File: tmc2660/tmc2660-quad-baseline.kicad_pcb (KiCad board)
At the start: 4 copper layers, 125 x 40 mm, 79 parts, among them J1 Power, J100 0R, J2 DataIn, J200 0R, J300 0R, J400 0R, M0 Mount, M1 Mount, M100 Mount, M101 Mount, M200 Mount, M201 Mount, M300 Mount, M301 Mount, M400 Mount, M401 Mount, P100 Motor, P200 Motor, P300 Motor, P400 Motor, U100 TMC2660, U200 TMC2660, U300 TMC2660, U400 TMC2660

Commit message: Add bottom silkscreen.
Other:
- board text added: "%%gitversion%%"
- board text added: "http://quadrigotion.org/"
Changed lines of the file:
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@@
   (general
     (thickness 1.6)
-    (drawings 29)
+    (drawings 31)
     (tracks 189)
     (zones 0)
@@
     (effects (font (size 2.2 2.2) (thickness 0.4)))
   )
+  (gr_text http://quadrigotion.org/ (at 198.3645 94.732) (layer B.SilkS)
+    (effects (font (size 1.2 1.2) (thickness 0.2)) (justify left mirror))
+  )
+  (gr_text %%gitversion%% (at 112.5125 94.732) (layer B.SilkS)
+    (effects (font (size 1.2 1.2) (thickness 0.2)) (justify mirror))
+  )
   (gr_arc (start 211.2 61.934) (end 213.2 61.934) (angle -90) (layer Edge.Cuts) (width 0.1))

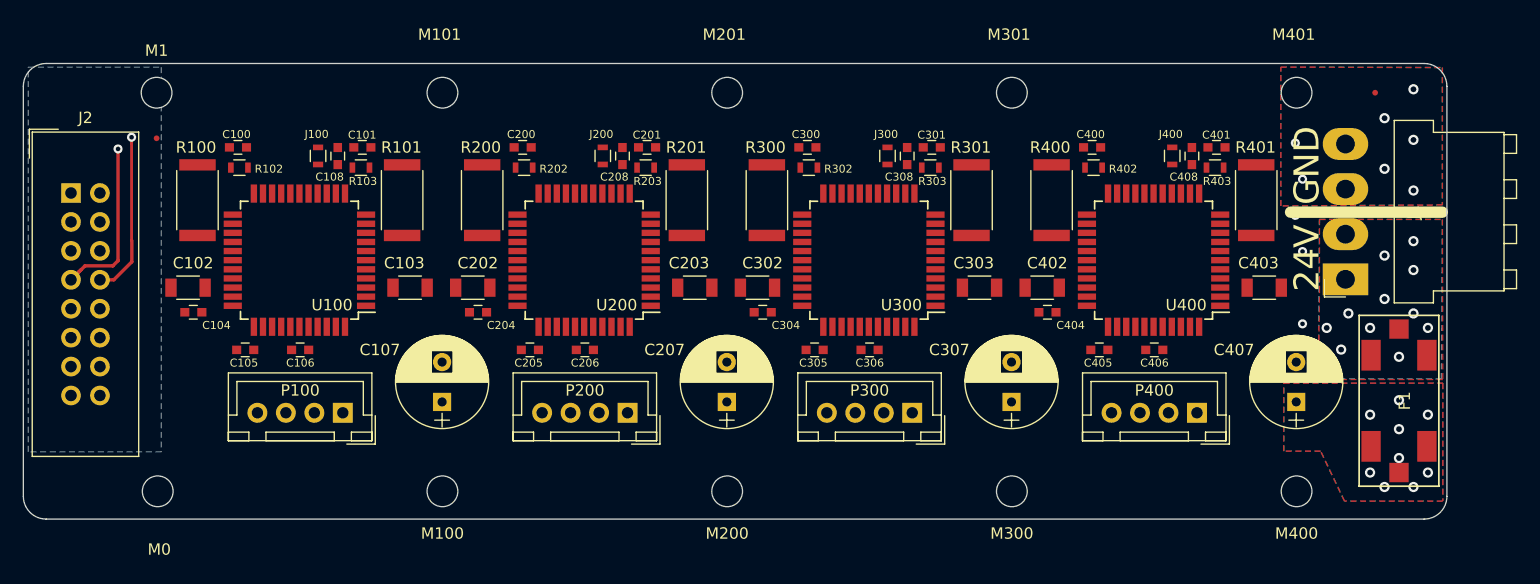
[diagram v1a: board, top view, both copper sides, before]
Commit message: Add front silkscreen. Re-add center fiducial.
o Front silkscreen and center fiducial got lost in the previous
  steps.
o Re-add in the baseline file and re-generate the final file.
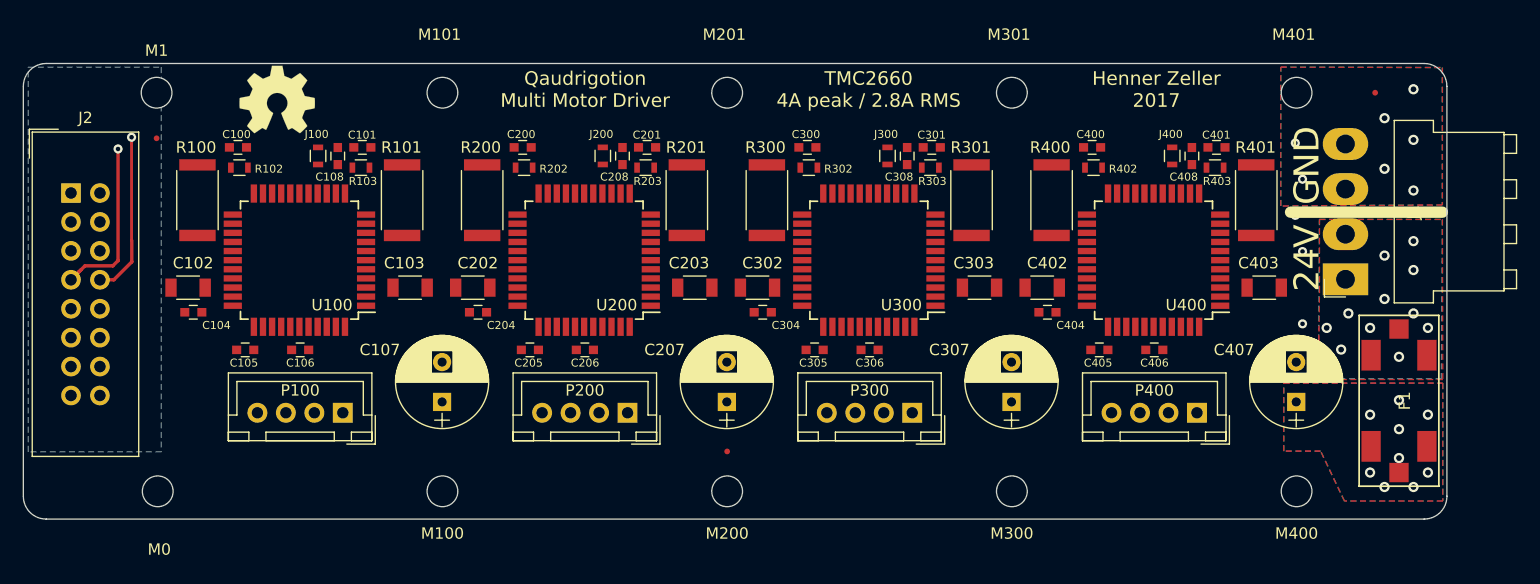
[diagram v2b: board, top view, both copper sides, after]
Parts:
- added REF**: Fiducial_0.5mm_Dia_1mm_Outer, Fiducials:Fiducial_0.5mm_Dia_1mm_Outer, F.Cu at (150.0, 94.0)
- added REF***: OSHW-Symbol_6.7x6mm_SilkScreen, Symbols:OSHW-Symbol_6.7x6mm_SilkScreen, F.Cu at (110.5, 63.1)
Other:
- board text added: "Henner Zeller 2017"
- board text added: "Qaudrigotion Multi Motor Driver"
- board text added: "TMC2660 4A peak / 2.8A RMS"

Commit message: GND plane around Step/Dir. Tighter routing of Step/Dir.
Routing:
- net DIR4: track 104.2 -> 104.8 mm
- net GND: vias 10 -> 9
- net GLOBAL_MOSI: vias 1 -> 2
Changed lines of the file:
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@@
     (thickness 1.6)
     (drawings 34)
-    (tracks 189)
+    (tracks 188)
     (zones 0)
     (modules 81)
@@
   (gr_line (start 88.2 97.939) (end 88.2 61.934) (layer Edge.Cuts) (width 0.1))
   (gr_line (start 211.2 99.939) (end 90.2 99.939) (layer Edge.Cuts) (width 0.1))
-  (via (at 199.8885 66.919) (size 0.8) (drill 0.4) (layers F.Cu B.Cu) (net 1))
+  (segment (start 189.7285 82.74601) (end 190.28449 83.302) (width 0.25) (layer In1.Cu) (net 51))
+  (segment (start 169.102489 84.497011) (end 170.85349 82.74601) (width 0.25) (layer In1.Cu) (net 51))
+  (segment (start 166.463458 83.82691) (end 167.133559 84.497011) (width 0.25) (layer In1.Cu) (net 51))
+  (segment (start 145.89659 83.82691) (end 166.463458 83.82691) (width 0.25) (layer In1.Cu) (net 51))
+  (segment (start 144.24559 85.47791) (end 145.89659 83.82691) (width 0.25) (layer In1.Cu) (net 51))
+  (segment (start 141.16511 85.47791) (end 144.24559 85.47791) (width 0.25) (layer In1.Cu) (net 51))
+  (segment (start 103.2721 84.4149) (end 104.519259 85.662059) (width 0.25) (layer In1.Cu) (net 51))
+  (segment (start 170.85349 82.74601) (end 189.7285 82.74601) (width 0.25) (layer In1.Cu) (net 51))
+  (segment (start 140.27611 84.58891) (end 141.16511 85.47791) (width 0.25) (layer In1.Cu) (net 51))
+  (segment (start 121.184452 84.58891) (end 140.27611 84.58891) (width 0.25) (layer In1.Cu) (net 51))
+  (segment (start 167.133559 84.497011) (end 169.102489 84.497011) (width 0.25) (layer In1.Cu) (net 51))
+  (segment (start 102.8591 84.4149) (end 103.2721 84.4149) (width 0.25) (layer In1.Cu) (net 51))
+  (segment (start 119.423423 86.349939) (end 121.184452 84.58891) (width 0.25) (layer In1.Cu) (net 51))
+  (segment (start 104.519259 85.662059) (end 114.933259 85.662059) (width 0.25) (layer In1.Cu) (net 51))
+  (segment (start 114.933259 85.662059) (end 115.621139 86.349939) (width 0.25) (layer In1.Cu) (net 51))
+  (segment (start 115.621139 86.349939) (end 119.423423 86.349939) (width 0.25) (layer In1.Cu) (net 51))
+  (segment (start 190.28449 83.302) (end 193.1308 83.302) (width 0.25) (layer In1.Cu) (net 51))
+  (segment (start 168.800499 84.037001) (end 170.5515 82.286) (width 0.25) (layer In1.Cu) (net 52))
+  (segment (start 170.5515 82.286) (end 193.1435 82.286) (width 0.25) (layer In1.Cu) (net 52))
+  (segment (start 166.654 83.3669) (end 167.324101 84.037001) (width 0.25) (layer In1.Cu) (net 52))
+  (segment (start 167.324101 84.037001) (end 168.800499 84.037001) (width 0.25) (layer In1.Cu) (net 52))
+  (via (at 199.8885 66.919) (size 0.8) (drill 0.4) (layers F.Cu B.Cu) (net 55))
   (via (at 200.5235 70.094) (size 0.8) (drill 0.4) (layers F.Cu B.Cu) (net 1))
   (via (at 199.8885 73.269) (size 0.8) (drill 0.4) (layers F.Cu B.Cu) (net 1))
@@
   (segment (start 103.806822 83.2549) (end 98.2166 83.2549) (width 0.25) (layer In1.Cu) (net 38))
   (segment (start 98.2166 83.2549) (end 94.9245 86.547) (width 0.25) (layer In1.Cu) (net 38))
-  (segment (start 145.419652 84.2559) (end 144.197642 85.47791) (width 0.25) (layer In1.Cu) (net 51))
-  (segment (start 168.407254 84.7639) (end 154.9291 84.7639) (width 0.25) (layer In1.Cu) (net 51))
-  (segment (start 140.27611 84.58891) (end 121.184452 84.58891) (width 0.25) (layer In1.Cu) (net 51))
-  (segment (start 154.4211 84.2559) (end 145.419652 84.2559) (width 0.25) (layer In1.Cu) (net 51))
-  (segment (start 154.9291 84.7639) (end 154.4211 84.2559) (width 0.25) (layer In1.Cu) (net 51))
-  (segment (start 115.621139 86.349939) (end 114.933259 85.662059) (width 0.25) (layer In1.Cu) (net 51))
-  (segment (start 193.1308 83.302) (end 169.869154 83.302) (width 0.25) (layer In1.Cu) (net 51))
-  (segment (start 169.869154 83.302) (end 168.407254 84.7639) (width 0.25) (layer In1.Cu) (net 51))
-  (segment (start 144.197642 85.47791) (end 141.16511 85.47791) (width 0.25) (layer In1.Cu) (net 51))
-  (segment (start 141.16511 85.47791) (end 140.27611 84.58891) (width 0.25) (layer In1.Cu) (net 51))
-  (segment (start 114.933259 85.662059) (end 104.519259 85.662059) (width 0.25) (layer In1.Cu) (net 51))
-  (segment (start 121.184452 84.58891) (end 119.423423 86.349939) (width 0.25) (layer In1.Cu) (net 51))
-  (segment (start 119.423423 86.349939) (end 115.621139 86.349939) (width 0.25) (layer In1.Cu) (net 51))
-  (segment (start 104.519259 85.662059) (end 103.2721 84.4149) (width 0.25) (layer In1.Cu) (net 51))
-  (segment (start 103.2721 84.4149) (end 102.8591 84.4149) (width 0.25) (layer In1.Cu) (net 51))
   (segment (start 102.8591 84.4149) (end 98.6471 84.4149) (width 0.25) (layer In1.Cu) (net 51))
   (segment (start 103.0971 84.4149) (end 102.8591 84.4149) (width 0.25) (layer In1.Cu) (net 51))
@@
   (segment (start 96.583112 86.478888) (end 96.583112 87.428388) (width 0.25) (layer In1.Cu) (net 51))
   (segment (start 96.583112 87.428388) (end 95.788099 88.223401) (width 0.25) (layer In1.Cu) (net 51))
-  (segment (start 144.0071 85.0179) (end 141.4671 85.0179) (width 0.25) (layer In1.Cu) (net 52))
-  (segment (start 141.4671 85.0179) (end 140.5781 84.1289) (width 0.25) (layer In1.Cu) (net 52))
-  (segment (start 115.696593 85.202049) (end 105.075249 85.202049) (width 0.25) (layer In1.Cu) (net 52))
-  (segment (start 116.384473 85.889929) (end 115.696593 85.202049) (width 0.25) (layer In1.Cu) (net 52))
-  (segment (start 93.725899 87.745601) (end 93.248099 88.223401) (width 0.25) (layer In1.Cu) (net 52))
-  (segment (start 140.5781 84.1289) (end 120.99391 84.1289) (width 0.25) (layer In1.Cu) (net 52))
-  (segment (start 145.6581 83.3669) (end 144.0071 85.0179) (width 0.25) (layer In1.Cu) (net 52))
-  (segment (start 157.5961 83.3669) (end 145.6581 83.3669) (width 0.25) (layer In1.Cu) (net 52))
-  (segment (start 103.7081 83.8349) (end 98.3071 83.8349) (width 0.25) (layer In1.Cu) (net 52))
-  (segment (start 193.1435 82.286) (end 169.8502 82.286) (width 0.25) (layer In1.Cu) (net 52))
-  (segment (start 119.232881 85.889929) (end 116.384473 85.889929) (width 0.25) (layer In1.Cu) (net 52))
-  (segment (start 96.123101 87.122329) (end 95.499829 87.745601) (width 0.25) (layer In1.Cu) (net 52))
-  (segment (start 120.99391 84.1289) (end 119.232881 85.889929) (width 0.25) (layer In1.Cu) (net 52))
-  (segment (start 169.8502 82.286) (end 168.865801 83.270399) (width 0.25) (layer In1.Cu) (net 52))
-  (segment (start 168.865801 83.270399) (end 168.865801 83.654801) (width 0.25) (layer In1.Cu) (net 52))
-  (segment (start 168.865801 83.654801) (end 168.483601 84.037001) (width 0.25) (layer In1.Cu) (net 52))
-  (segment (start 168.483601 84.037001) (end 158.266201 84.037001) (width 0.25) (layer In1.Cu) (net 52))
-  (segment (start 158.266201 84.037001) (end 157.5961 83.3669) (width 0.25) (layer In1.Cu) (net 52))
-  (segment (start 105.075249 85.202049) (end 103.7081 83.8349) (width 0.25) (layer In1.Cu) (net 52))
-  (segment (start 98.3071 83.8349) (end 96.123101 86.018899) (width 0.25) (layer In1.Cu) (net 52))
-  (segment (start 96.123101 86.018899) (end 96.123101 87.122329) (width 0.25) (layer In1.Cu) (net 52))
-  (segment (start 95.499829 87.745601) (end 93.725899 87.745601) (width 0.25) (layer In1.Cu) (net 52))
-  (segment (start 93.248099 88.223401) (end 92.3845 89.087) (width 0.25) (layer In1.Cu) (net 52))
+  (segment (start 145.6581 83.3669) (end 166.654 83.3669) (width 0.25) (layer In1.Cu) (net 52))
+  (segment (start 141.4671 85.0179) (end 144.0071 85.0179) (width 0.25) (layer In1.Cu) (net 52))
+  (segment (start 140.5781 84.1289) (end 141.4671 85.0179) (width 0.25) (layer In1.Cu) (net 52))
+  (segment (start 144.0071 85.0179) (end 145.6581 83.3669) (width 0.25) (layer In1.Cu) (net 52))
+  (segment (start 120.99391 84.1289) (end 140.5781 84.1289) (width 0.25) (layer In1.Cu) (net 52))
+  (segment (start 119.232881 85.889929) (end 120.99391 84.1289) (width 0.25) (layer In1.Cu) (net 52))
+  (segment (start 116.384473 85.889929) (end 119.232881 85.889929) (width 0.25) (layer In1.Cu) (net 52))
+  (segment (start 103.7081 83.8349) (end 105.075249 85.202049) (width 0.25) (layer In1.Cu) (net 52))
+  (segment (start 93.725899 87.745601) (end 95.499829 87.745601) (width 0.25) (layer In1.Cu) (net 52))
+  (segment (start 92.3845 89.087) (end 93.725899 87.745601) (width 0.25) (layer In1.Cu) (net 52))
+  (segment (start 95.499829 87.745601) (end 96.123101 87.122329) (width 0.25) (layer In1.Cu) (net 52))
+  (segment (start 96.123101 87.122329) (end 96.123101 86.018899) (width 0.25) (layer In1.Cu) (net 52))
+  (segment (start 105.075249 85.202049) (end 115.696593 85.202049) (width 0.25) (layer In1.Cu) (net 52))
+  (segment (start 96.123101 86.018899) (end 98.3071 83.8349) (width 0.25) (layer In1.Cu) (net 52))
+  (segment (start 115.696593 85.202049) (end 116.384473 85.889929) (width 0.25) (layer In1.Cu) (net 52))
+  (segment (start 98.3071 83.8349) (end 103.7081 83.8349) (width 0.25) (layer In1.Cu) (net 52))
   (segment (start 97.7235 77.349314) (end 96.145814 78.927) (width 0.3) (layer F.Cu) (net 55))
   (segment (start 96.145814 78.927) (end 94.9245 78.927) (width 0.3) (layer F.Cu) (net 55))
@@
       )
     )
+  )
+  (zone (net 1) (net_name GND) (layer In1.Cu) (hatch edge 0.508)
+    (connect_pads (clearance 0.254))
+    (min_thickness 0.254)
+    (fill yes (arc_segments 16) (thermal_gap 0.508) (thermal_bridge_width 0.508))
+    (polygon
+      (pts
+        (xy 99.4315 78.984) (xy 201.5395 78.984) (xy 201.5395 87.112) (xy 99.4315 87.112)
+      )
+    )

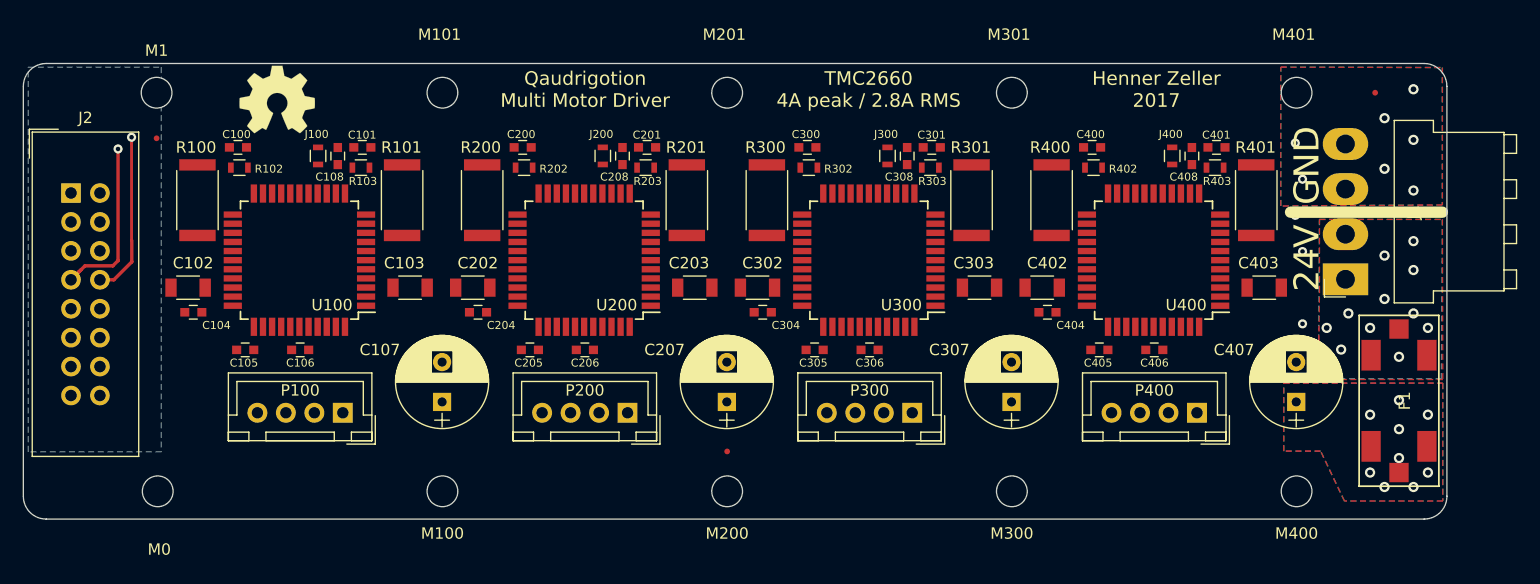
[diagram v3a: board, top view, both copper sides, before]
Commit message: Integrate grounded mounting hole.
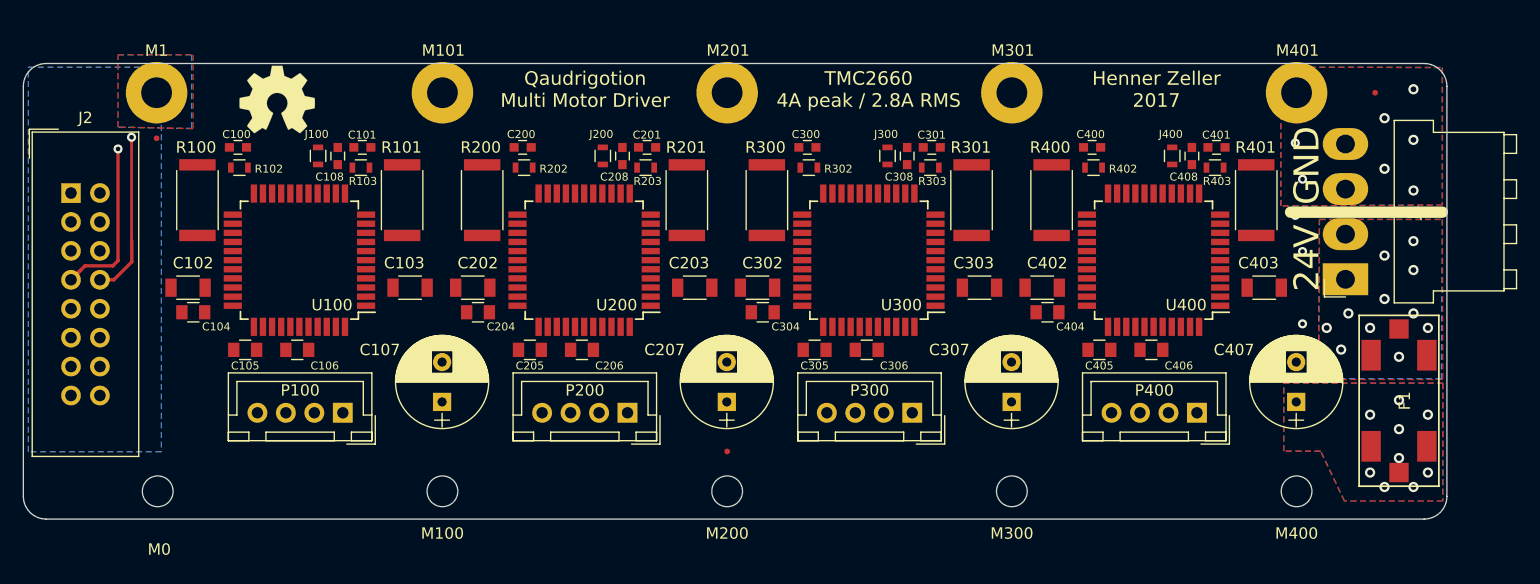
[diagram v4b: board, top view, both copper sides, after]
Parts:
- C104, C105, C106, C204, C205, C206, C304, C305, C306, C404, C405, C406: footprint Capacitors_SMD:C_0603 -> Capacitors_SMD:C_0805
- M1, M101, M201, M301, M401: footprint Mounting_Holes:MountingHole_2.7mm_M2.5 -> Mounting_Holes:MountingHole_2.7mm_M2.5_Pad
- moved C106 0.25 mm to (112.3, 85.1)
- moved C206 0.25 mm to (137.3, 85.1)
- moved C306 0.25 mm to (162.3, 85.1)
- moved C406 0.25 mm to (187.3, 85.1)
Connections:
- M1 pad 1: (no net) -> GND
- M101 pad 1: (no net) -> GND
- M201 pad 1: (no net) -> GND
- M301 pad 1: (no net) -> GND
- M401 pad 1: (no net) -> GND

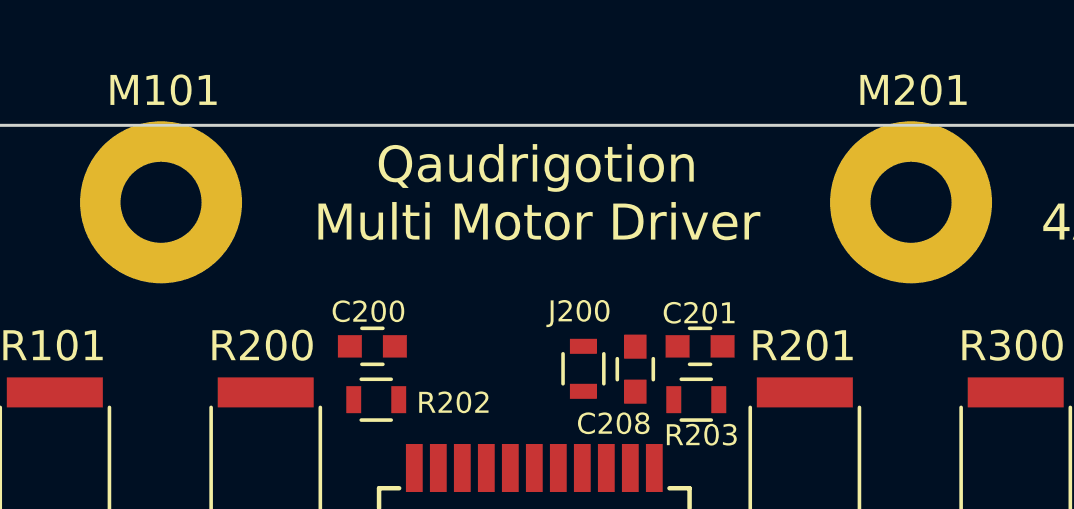
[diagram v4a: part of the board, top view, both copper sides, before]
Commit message: Silk screen: http://quadrigotion.org/ on front; github ref on back.
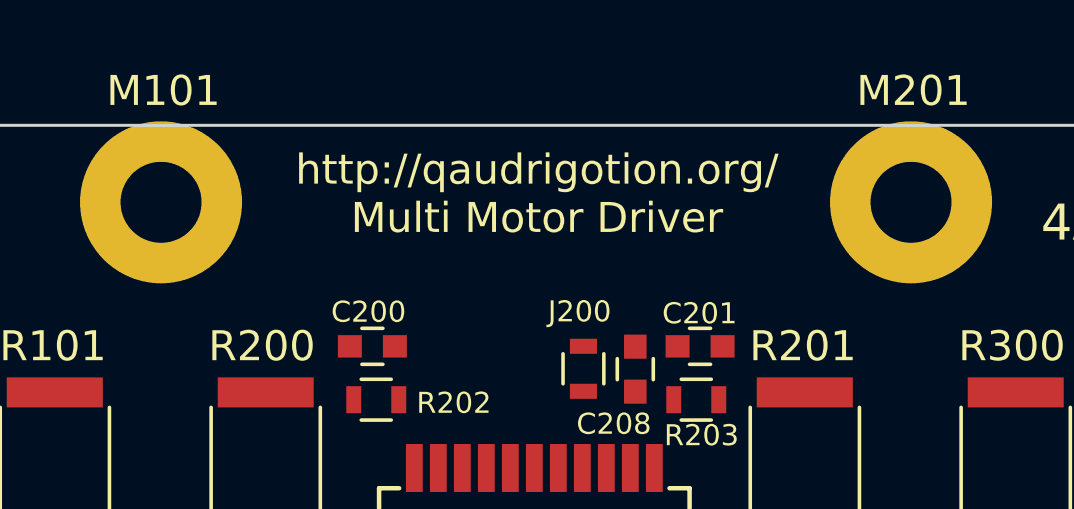
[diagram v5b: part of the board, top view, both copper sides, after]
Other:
- board text added: "http://qaudrigotion.org/ Multi Motor Driver"
- board text added: "https://github.com/hzeller/quadrigotion"
- board text removed: "Qaudrigotion Multi Motor Driver"
- board text removed: "http://quadrigotion.org/"
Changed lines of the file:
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@@
     (effects (font (size 1.2 1.2) (thickness 0.2)))
   )
-  (gr_text "Qaudrigotion\nMulti Motor Driver" (at 137.5315 62.22) (layer F.SilkS)
-    (effects (font (size 1.2 1.2) (thickness 0.2)))
+  (gr_text "http://qaudrigotion.org/\nMulti Motor Driver" (at 137.5315 62.22) (layer F.SilkS)
+    (effects (font (size 1 1) (thickness 0.2)))
   )
   (gr_text GND (at 200.9031 68.8889 90) (layer F.SilkS)
@@
     (effects (font (size 2.2 2.2) (thickness 0.4)))
   )
-  (gr_text http://quadrigotion.org/ (at 198.3645 94.732) (layer B.SilkS)
+  (gr_text https://github.com/hzeller/quadrigotion (at 198.3645 94.732) (layer B.SilkS)
     (effects (font (size 1.2 1.2) (thickness 0.2)) (justify left mirror))
   )
